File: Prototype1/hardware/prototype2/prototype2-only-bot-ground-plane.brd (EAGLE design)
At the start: 101.6 x 75.9 mm, 94 parts, among them IC1 ATTINY13A-SSU, IC2 LDL112D33R, IC3 FT2232HL-REEL, IC4 93LC46BT-I_OT, IC5 APA104, IC6 APA104, IC7 APA104, IC8 APA104, J4 DN PAIR, U2 ESP-WROOM-32

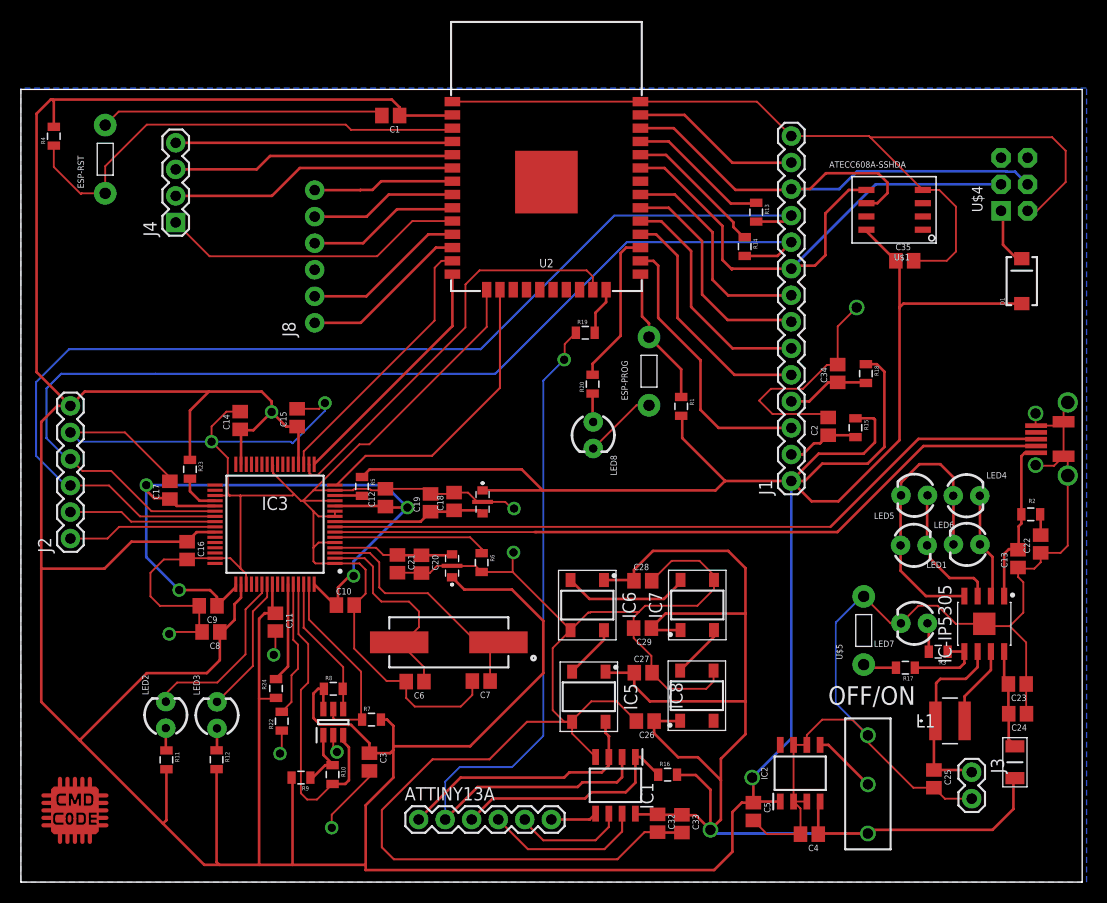
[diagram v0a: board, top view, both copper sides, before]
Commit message: shorten board a bit so it fits on a 3x4 f4 board
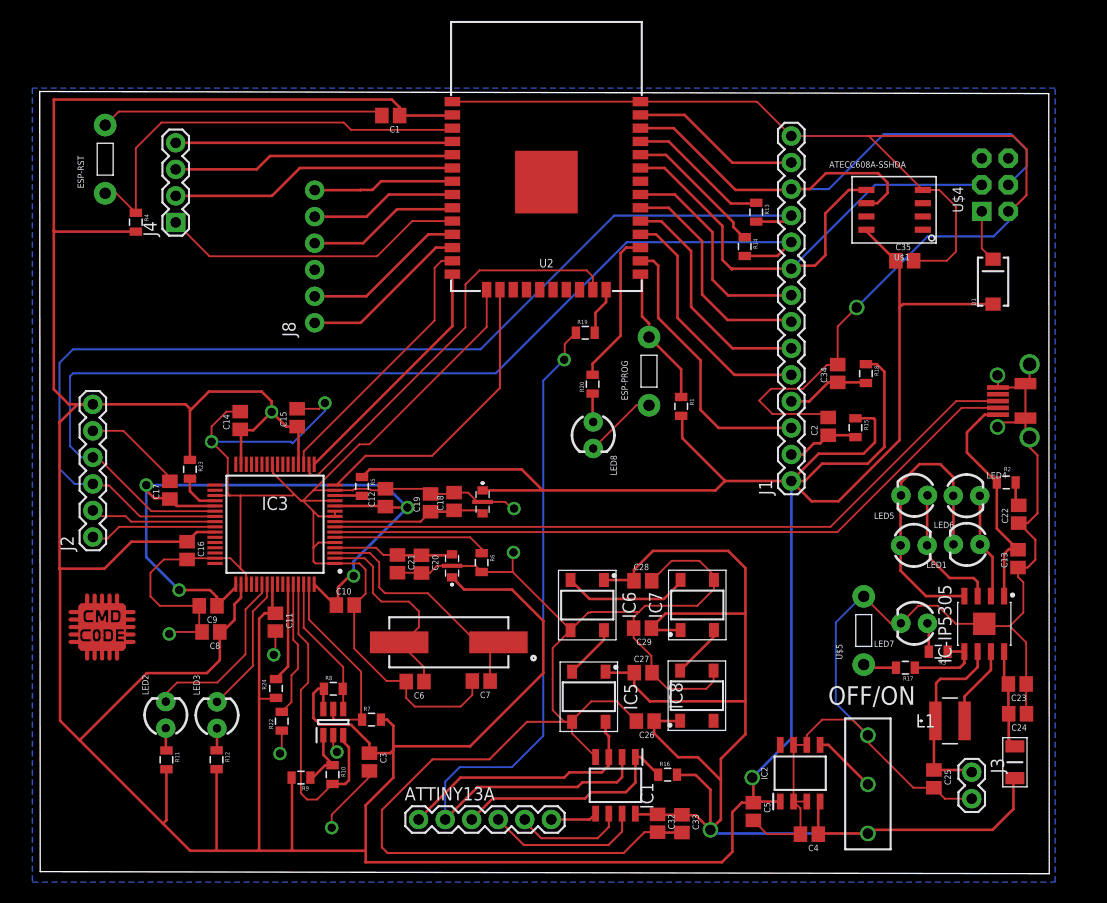
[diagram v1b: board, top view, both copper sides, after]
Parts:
- moved U$3 17.7 mm to (7.77, 24.7)
- moved R4 11.4 mm to (11.0, 63.2), turned to 270 degrees
- moved U$2 5.16 mm to (92.8, 46.1)
- moved R2 3.85 mm to (94.3, 38.2)
- moved C22 3.54 mm to (95.5, 35.2)
- moved D1 2.75 mm to (93.0, 57.5)
- moved J2 2.16 mm to (6.89, 33.0)
- moved U$4 1.85 mm to (93.2, 66.7)
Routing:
- net VCC: track 556.9 -> 547.9 mm
- net VCC5V: track 16.2 -> 22.6 mm
- net SCL: track 54.4 -> 60.0 mm
- net ESP-EN: track 45.8 -> 41.6 mm
- net TXD_SPI_PROM_CLK: track 105.9 -> 102.5 mm
- net RXD_SPI_PROM_MOSI: track 109.1 -> 106.4 mm
- net GND: track 596.0 -> 598.3 mm
- net USB_DP: track 70.6 -> 68.4 mm
- net USB_DM: track 70.5 -> 68.4 mm
- net SPI_PROM_MISO: track 14.2 -> 12.1 mm
- net SPI_PROM_CS: track 14.3 -> 12.2 mm
- net SDA: track 56.5 -> 54.6 mm
- net N$1: track 5.68 -> 5.06 mm
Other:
- board size 101.6 x 75.9 mm -> 96.6 x 74.9 mm

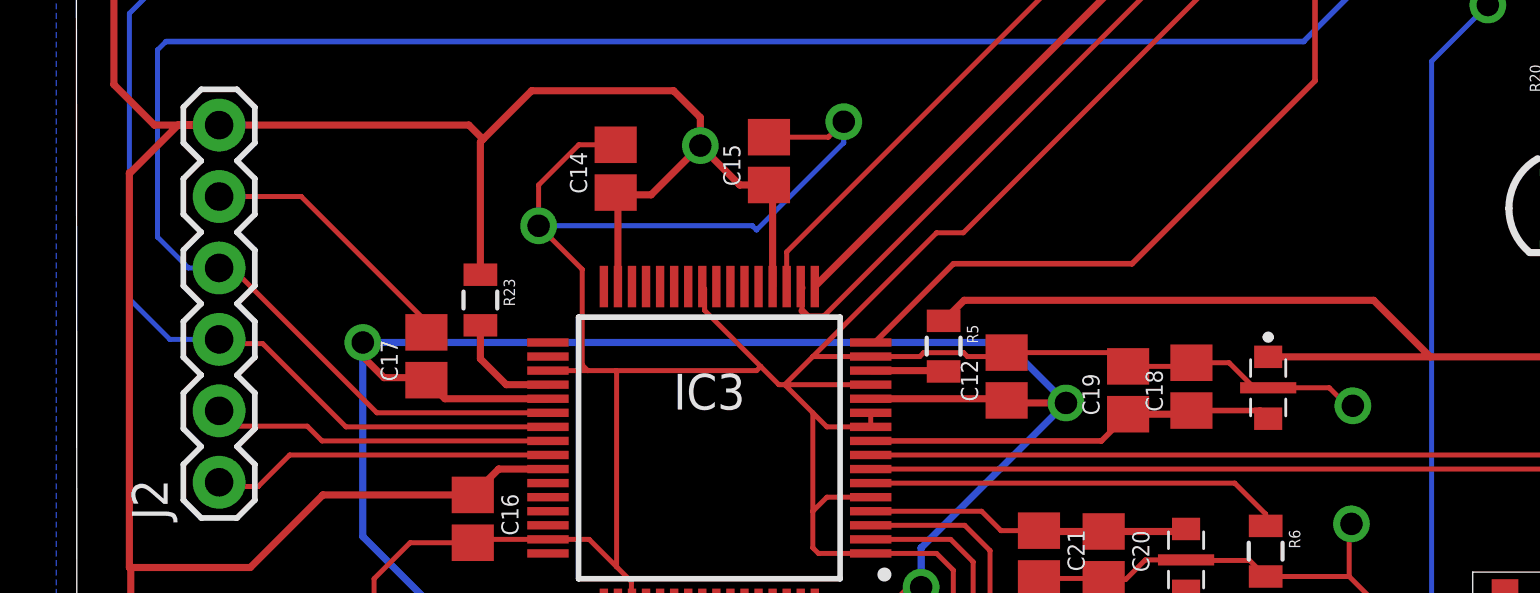
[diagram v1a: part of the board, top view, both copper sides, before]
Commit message: removing bad file location and fixing a missing ground
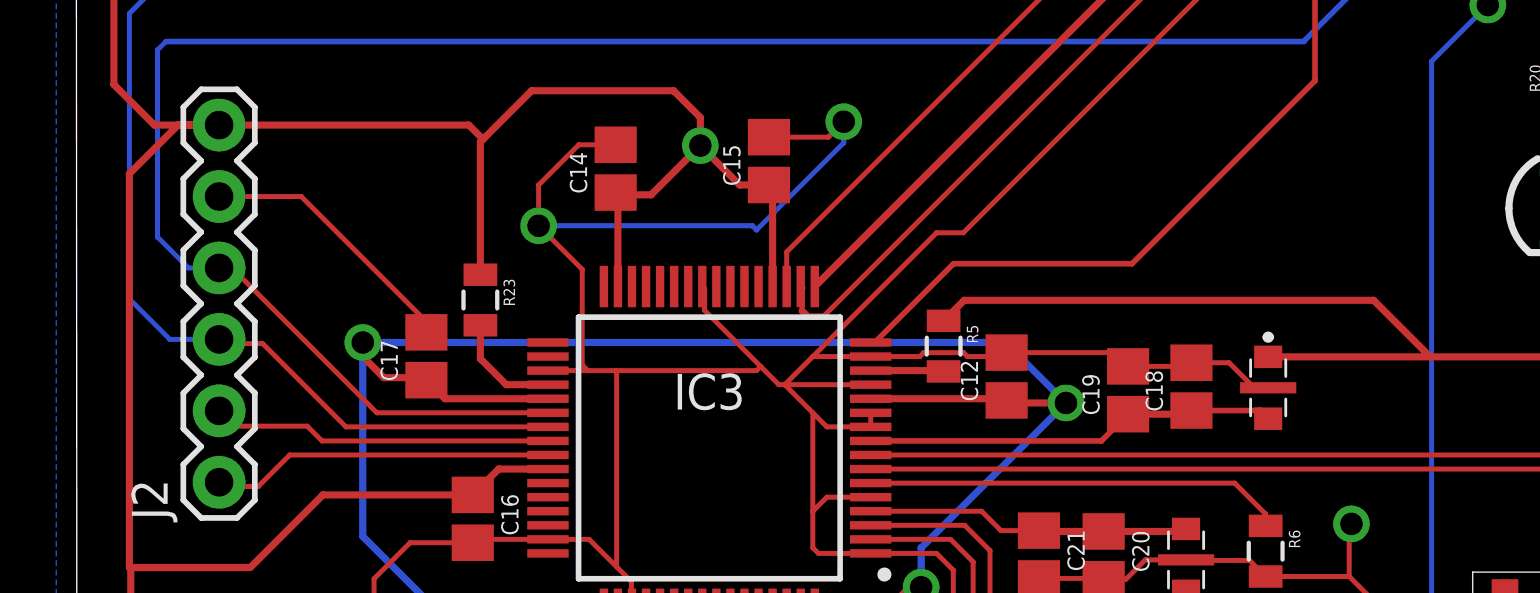
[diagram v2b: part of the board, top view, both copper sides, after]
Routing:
- net GND: track 598.3 -> 596.5 mm, vias 10 -> 9
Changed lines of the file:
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@@
 <wire x1="3.75" y1="15.45" x2="3.75" y2="30" width="0.254" layer="1"/>
 <wire x1="3.7" y1="30" x2="3.7" y2="44" width="0.254" layer="1"/>
-<wire x1="3.7" y1="44" x2="3.7" y2="44.05" width="0.254" layer="1"/>
 <wire x1="69" y1="7.6" x2="68.1" y2="6.7" width="0.254" layer="1"/>
 <wire x1="67.1" y1="1.9" x2="33" y2="1.9" width="0.254" layer="1"/>
@@
 <wire x1="14.2" y1="23.75" x2="14.39" y2="23.94" width="0.1778" layer="1"/>
 <wire x1="14.39" y1="23.94" x2="17.34" y2="23.94" width="0.1778" layer="1"/>
-<via x="47.2" y="35.75" extent="1-16" drill="0.8"/>
-<wire x1="44.69" y1="36.39" x2="46.36" y2="36.39" width="0.1778" layer="1"/>
-<wire x1="47" y1="35.75" x2="47.2" y2="35.75" width="0.1778" layer="1"/>
-<wire x1="46.36" y1="36.39" x2="47" y2="35.75" width="0.1778" layer="1"/>
 <wire x1="30.058" y1="35.5" x2="30.058" y2="35" width="0.1778" layer="1"/>
 <via x="18.25" y="42.15" extent="1-16" drill="0.8"/>
@@
 <wire x1="9.81" y1="43.19" x2="6.89" y2="43.19" width="0.1778" layer="1"/>
 <wire x1="14.26" y1="38.74" x2="9.81" y2="43.19" width="0.1778" layer="1"/>
+<wire x1="43.69" y1="36.39" x2="44.69" y2="36.39" width="0.1778" layer="1"/>
 </signal>
 <signal name="DISPLAY_CS">

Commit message: increased width of traces and tried a different package for slide switch
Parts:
- C1, C13, C22, C23, C24, C25: value 10 uf -> 10 uF
- CHARGE-VOLTAGE: value SWITCH_TACTILETACTILE-2PIN-NARROW -> UserButton
- OFF/ON: device switches:SWITCH-SPDT -> switches:SWITCH-SPDT_LOCK.007S
- R10: value 2.2K -> 2.2 K
- R11, R12: value 56 -> 56 R
- R22: value 4.7K -> 4.7 K
- R5: value 1K -> 1 K
- renumbered U$5 to CHARGE-VOLTAGE
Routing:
- net GND: track 596.5 -> 594.4 mm
- net VBAT: track 138.8 -> 140.2 mm

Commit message: fixed bug with center ground plane on esp32
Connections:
- net GND: now also U2.GND
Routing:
- net GND: track 594.4 -> 601.9 mm
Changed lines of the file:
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@@
 <wire x1="21.023334375" y1="30.023334375" x2="21.55" y2="29.49666875" width="0.254" layer="1"/>
 <wire x1="18.582" y1="31" x2="20.04666875" y2="31" width="0.254" layer="1"/>
-<wire x1="95.44" y1="30.11" x2="95.45" y2="30.1" width="0.1778" layer="1"/>
 <wire x1="80.67" y1="27.3439" x2="83.2439" y2="24.77" width="0.1778" layer="1"/>
 <wire x1="83.2439" y1="24.77" x2="84.23" y2="24.77" width="0.1778" layer="1"/>
@@
 <wire x1="89.48" y1="24.72" x2="92.05" y2="24.72" width="0.1778" layer="1"/>
 <wire x1="92.05" y1="24.72" x2="92.21" y2="24.72" width="0.1778" layer="1"/>
-<wire x1="92.21" y1="24.72" x2="92.43" y2="24.5" width="0.1778" layer="1"/>
 <wire x1="81.07" y1="12.0678" x2="78" y2="17.12" width="0.508" layer="16"/>
 <wire x1="78" y1="17.12" x2="78" y2="24.85" width="0.508" layer="16"/>
@@
 <wire x1="9.3661" y1="73.75" x2="8.07" y2="72.4539" width="0.1778" layer="1"/>
 <wire x1="34.17" y1="73.75" x2="9.3661" y2="73.75" width="0.1778" layer="1"/>
-<wire x1="41.3" y1="74.7" x2="59.3" y2="74.7" width="0.1778" layer="1"/>
 <wire x1="59.3" y1="74.7" x2="70.45" y2="74.7" width="0.254" layer="1"/>
 <wire x1="70.45" y1="74.7" x2="73.74" y2="71.41" width="0.254" layer="1"/>
@@
 <wire x1="97.3" y1="35.3" x2="96.36" y2="34.36" width="0.254" layer="1"/>
 <wire x1="96.36" y1="34.36" x2="95.51" y2="34.36" width="0.254" layer="1"/>
-<wire x1="95.44" y1="30.11" x2="96.36" y2="30.11" width="0.254" layer="1"/>
 <wire x1="96.36" y1="30.11" x2="97.1" y2="30.85" width="0.254" layer="1"/>
 <wire x1="97.1" y1="30.85" x2="97.1" y2="32.77" width="0.254" layer="1"/>
@@
 <wire x1="87.39" y1="9.03" x2="84.1078" y2="9.03" width="0.4064" layer="1"/>
 <wire x1="84.1078" y1="9.03" x2="81.07" y2="12.0678" width="0.4064" layer="1"/>
-<wire x1="95.44" y1="30.11" x2="95.44" y2="26.19" width="0.3048" layer="1"/>
 <wire x1="93.97" y1="24.72" x2="92.05" y2="24.72" width="0.3048" layer="1"/>
 <wire x1="95.44" y1="26.19" x2="93.97" y2="24.72" width="0.3048" layer="1"/>
@@
 <wire x1="96.22" y1="18.96" x2="96.22" y2="16.14" width="0.3048" layer="1"/>
 <wire x1="96.22" y1="16.14" x2="96.25" y2="16.11" width="0.3048" layer="1"/>
+<wire x1="95.44" y1="30.11" x2="96.36" y2="30.11" width="0.254" layer="1"/>
+<wire x1="95.44" y1="30.11" x2="95.44" y2="26.19" width="0.254" layer="1"/>
+<contactref element="U2" pad="GND"/>
+<wire x1="41.3" y1="74.7" x2="50" y2="74.7" width="0.508" layer="1"/>
+<wire x1="50" y1="74.7" x2="59.3" y2="74.7" width="0.508" layer="1"/>
+<wire x1="50.3" y1="67" x2="50.3" y2="74.4" width="0.508" layer="1"/>
+<wire x1="50.3" y1="74.4" x2="50" y2="74.7" width="0.508" layer="1"/>
+<wire x1="34.55" y1="73.37" x2="41.3" y2="74.7" width="0" layer="19" extent="1-1"/>
+<wire x1="60.12" y1="45.6361" x2="70.65875" y2="46.085" width="0" layer="19" extent="1-1"/>
+<wire x1="44.69" y1="36.39" x2="54.78" y2="41.5" width="0" layer="19" extent="1-1"/>
+<wire x1="36.04" y1="29.61" x2="32.9944" y2="29.9056" width="0" layer="19" extent="1-1"/>
+<wire x1="33.36" y1="10.06" x2="34.55" y2="6.9" width="0" layer="19" extent="1-1"/>
+<wire x1="30.25" y1="12.45" x2="33.36" y2="10.64" width="0" layer="19" extent="1-1"/>
+<wire x1="24.97" y1="12.47" x2="29.85" y2="12.9" width="0" layer="19" extent="1-1"/>
+<wire x1="28.55" y1="45.3" x2="32.4" y2="41.9" width="0" layer="19" extent="1-1"/>
+<wire x1="24.36" y1="24.03" x2="21.57" y2="28.512" width="0" layer="19" extent="1-1"/>
+<wire x1="70.11" y1="5.9" x2="63.27" y2="4.74" width="0" layer="19" extent="1-1"/>
+<wire x1="28.12" y1="58.61" x2="29.1" y2="45.85" width="0" layer="19" extent="1-1"/>
 </signal>
 <signal name="DISPLAY_CS" airwireshidden="yes">
